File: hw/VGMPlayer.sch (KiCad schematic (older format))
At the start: 91 parts, among them J1 Micro_SD_Card, J2 EarPiece, P1 USB_C_Receptacle_16P, P2 SWD, P3 BATT, P4 UART, P5 ICSP, P6 CODEC, Q1 2N7002, Q2 AO3401A, Q3 2N7002, U1 RP2040, U2 W25QxxJVZP, U3 TPS79933DDCR, U4 WM8978, U5 TP4057, U6 PIC16F1503-IMG, U7 TPS79933DDCR, Y1 12MHz

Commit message: 2nd version, change KBC functions
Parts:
- removed P2: SWD, BZ_Connector:PINHDR-THT-50mil-01x05, symbol BZ_Connector:Conn_01x05
- removed P4: UART, BZ_Connector:PINHDR-THT-50mil-01x02, symbol BZ_Connector:Conn_01x02
- removed R20: 1K, BZ_Resistor:R_0402, symbol BZ_Passive:R
- removed U5: TP4057, BZ_Standard_IC:SOT-23-6, symbol BZ_PMIC:TP4057
- added M1: Mechanical-NC, BZ_Mechanical:Hole-Mech_0.5, symbol BZ_Misc:Mechanical-NC
- added P2: SWD, BZ_Connector:PINHDR-THT-50mil-02x05, symbol BZ_Connector:Conn_02x05
- added R25, R26: 1K, BZ_Resistor:R_0402, symbol BZ_Passive:R
- added S5: RESET, BZ_Switch:C&K_PTS525, symbol BZ_Switch:PB-SPST-NO_2P
- added U5: MCP73831-OT, BZ_Standard_IC:SOT-23-5, symbol BZ_Microchip:MCP73831-OT
- C24, C34: value 10n -> DNP
- C25: value 4.7u -> 10u; JLCPN C1705 -> (none); PN CL10A475KP8NNNC -> GRM188R61A106KE69D
- C3, C4: value 33p -> 22p
- C35: value 4.7u -> 10u; JLCPN C1705 -> (none); PN CL10A475KP8NNNC -> (none)
- R10, R9: value 2K -> 2K2
- R20: renamed from R21; value 2K -> 2K2
- TP1: footprint BZ_Misc:TE_RCT0805 -> BZ_Misc:TP_THT-Pad-0.8
- TP2: value BAT+ -> TP; footprint BZ_Misc:TE_RCT0805 -> BZ_Misc:TP_THT-Pad-0.8
- TP3: value BAT- -> TP; footprint BZ_Misc:TE_RCT0805 -> BZ_Misc:TP_THT-Pad-0.8
- U3, U7: value TPS79933DDCR -> LP5907MFX-3.3; symbol BZ_TI:TPS79933DDCR -> BZ_TI:LP5907MFX
- renumbered R22 to R21, R23 to R22, R24 to R23, R25 to R24
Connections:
- net labels removed: CHG_CHRG
- wire segments 367 -> 377
- no-connect marks 22 -> 23
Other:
- moved on the sheet: C1, R18, R19, R3, S4, TP1, U2

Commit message: Using Molex Picoblade 1.25 connector
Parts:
- removed P3: BATT, BZ_Connector:JST_SM02B-SRSS-TB, symbol BZ_Connector:Conn_01x02_MP
- added P3: BATT, BZ_Connector:MLX_PicoBlade-Horz-01x02-1.25P, symbol BZ_Connector:Conn_01x02
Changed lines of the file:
@@
 	2350 1050 2450 1050
-Wire Wire Line
-	3650 1600 3650 1950
 Wire Wire Line
 	2750 5900 2850 5900
@@
 	3550 1300 3550 1150
 Connection ~ 3550 1150
-Wire Wire Line
-	3550 1600 3550 2050
 $Comp
 L BZ_Passive:C C17
@@
 	1    0    0    -1
 $EndComp
-$Comp
-L BZ_Connector:Conn_01x02_MP P3
-U 1 1 60A279CB
-P 2650 1000
-F 0 "P3" H 2700 1000 40  0000 L CNN
-F 1 "BATT" H 2700 1050 40  0000 L CNN
-F 2 "BZ_Connector:JST_SM02B-SRSS-TB" H 2650 950 40  0001 C CNN
-F 3 "~" H 2650 950 40  0001 C CNN
-	1    2650 1000
-	1    0    0    1
-$EndComp
-$Comp
-L BZ_Power:GND #PWR0106
-U 1 1 60AACCCE
-P 2650 1200
-F 0 "#PWR0106" H 2650 1200 30  0001 C CNN
-F 1 "GND" H 2650 1130 30  0001 C CNN
-F 2 "" H 2650 1200 60  0001 C CNN
-F 3 "" H 2650 1200 60  0001 C CNN
-	1    2650 1200
-	1    0    0    -1
-$EndComp
 Connection ~ 2800 1700
 $Comp
@@
 Wire Wire Line
 	3950 1600 4000 1600
-Wire Wire Line
-	3550 2050 3450 2050
-Wire Wire Line
-	3450 1950 3650 1950
 Wire Wire Line
 	5450 6600 5900 6600
@@
 	1150 5400 1250 5400
 NoConn ~ 1250 5700
+Wire Wire Line
+	3550 1600 3550 1950
+$Comp
+L BZ_Connector:Conn_01x02 P3
+U 1 1 60C059FA
+P 2650 1000
+F 0 "P3" H 2700 950 40  0000 L CNN
+F 1 "BATT" H 2700 1050 40  0000 L CNN
+F 2 "BZ_Connector:MLX_PicoBlade-Horz-01x02-1.25P" H 2650 950 40  0001 C CNN
+F 3 "~" H 2650 950 40  0001 C CNN
+	1    2650 1000
+	1    0    0    -1
+$EndComp
+Wire Wire Line
+	3550 1950 3450 1950
+Wire Wire Line
+	3650 2050 3450 2050
+Wire Wire Line
+	3650 1600 3650 2050
 $EndSCHEMATC

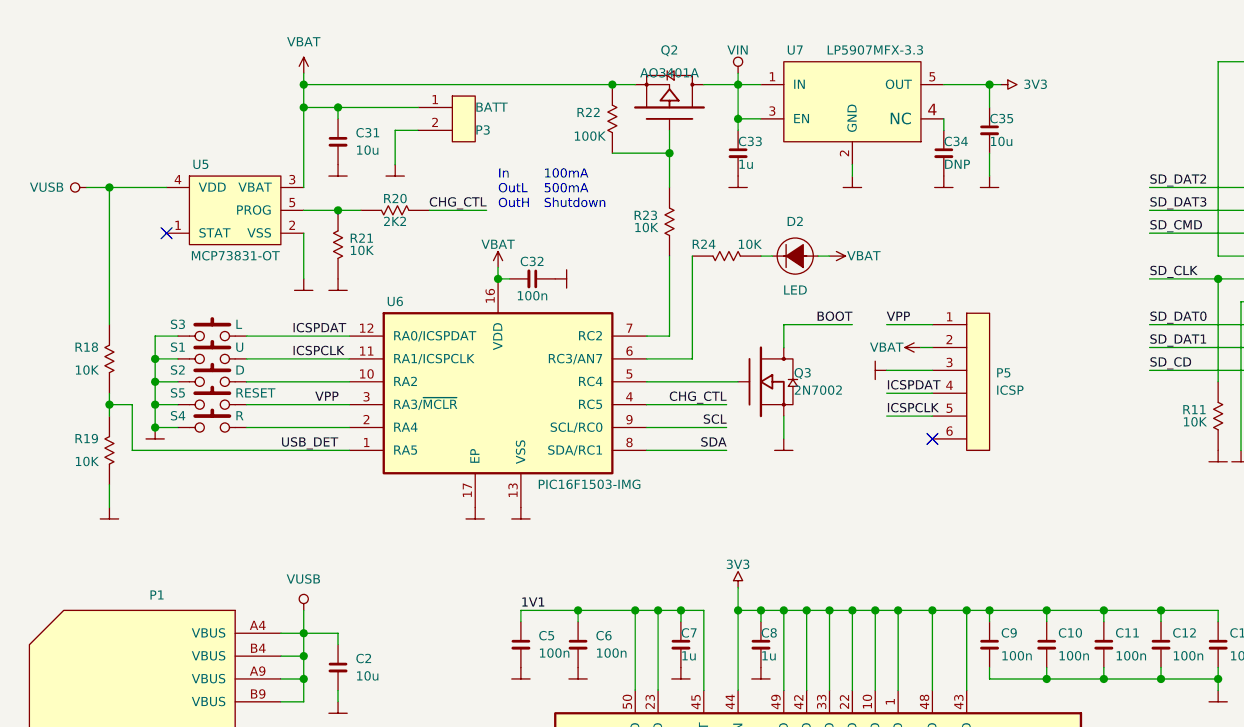
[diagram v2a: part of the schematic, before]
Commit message: USB/Batt power path
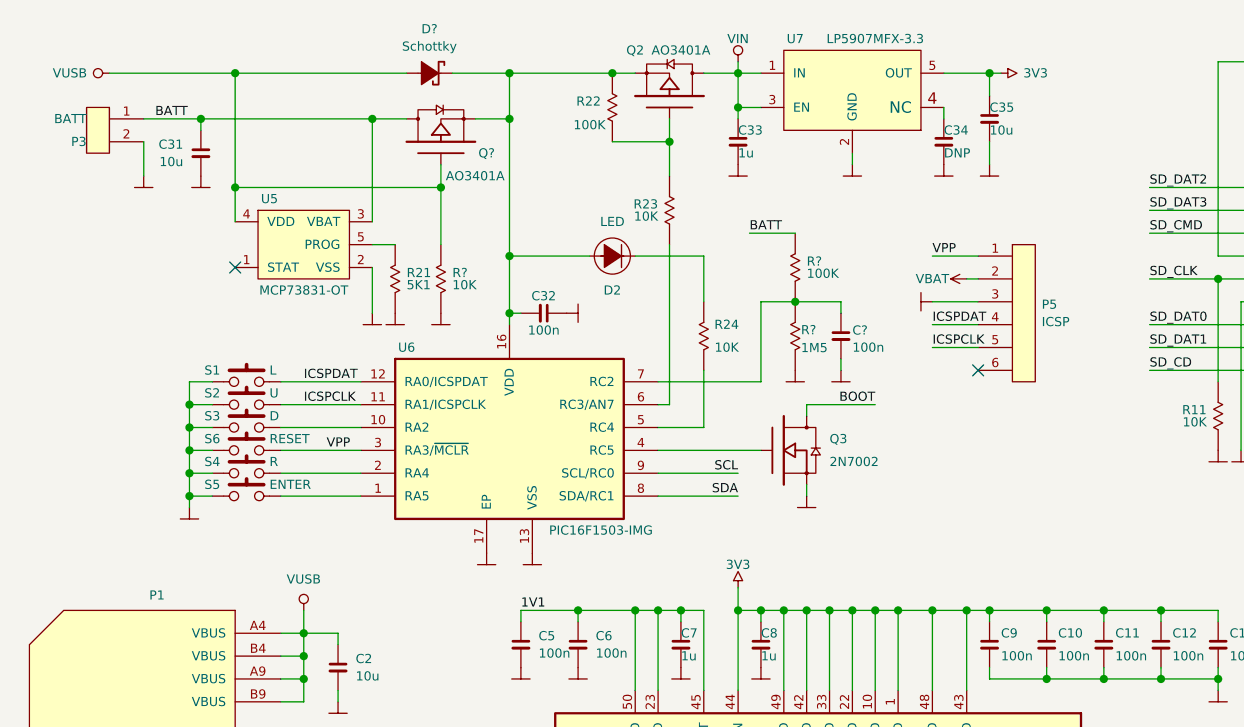
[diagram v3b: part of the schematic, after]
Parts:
- removed R18, R19: 10K, BZ_Resistor:R_0402, symbol BZ_Passive:R
- removed R20: 2K2, BZ_Resistor:R_0402, symbol BZ_Passive:R
- added C?: 100n, BZ_Capacitor:C_0402, symbol BZ_Passive:C
- added D?: Schottky, symbol BZ_Diode:Schottky
- added Q?: AO3401A, BZ_Standard_IC:SOT-23-3, symbol BZ_FET:MOS_P_GSD
- added R?: 10K, BZ_Resistor:R_0402, symbol BZ_Passive:R
- added R?: 100K, BZ_Resistor:R_0402, symbol BZ_Passive:R
- added R?: 1M5, BZ_Resistor:R_0402, symbol BZ_Passive:R
- added S5: ENTER, BZ_Switch:C&K_PTS525, symbol BZ_Switch:PB-SPST-NO_2P
- R21: value 10K -> 5K1
- renumbered S3 to S1, S1 to S2, S2 to S3, S5 to S6
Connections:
- net CHG_CTL is gone; now on an unnamed net: U6.4 (RC5)
- net GND: now also C?.2, R?.2, R?.2, S5.1
- net VBAT: no longer C31.1, C32.2, D2.A, P3.1 (Pin_1), Q2.2 (S), R22.1, U5.3 (VBAT), U6.16 (VDD)
- net VUSB: now also D?.A, Q?.1 (G), R?.1
- net at Q3.1 (G): no longer U6.5 (RC4)
- net at U6.6 (RC3/AN7): now also R23.2; no longer R24.2
- net at U6.7 (RC2): now also C?.1, R?.1, R?.2; no longer R23.2
- net at R24.1: now also U6.5 (RC4); no longer D2.K
- net USB_DET: no longer names the net of U6.1 (RA5)
- net USB_DET: now also S5.2
- new net: C32.2, D2.A, D?.K, Q2.2 (S), Q?.2 (S), R22.1, U6.16 (VDD)
- new net: D2.K, R24.2
- new net BATT: C31.1, P3.1 (Pin_1), Q?.3 (D), R?.1, U5.3 (VBAT)
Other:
- note removed: "100mA\n500mA\nShutdown"
- note removed: "In\nOutL\nOutH"
- moved on the sheet: C31, C32, C33, C34, C35, D2, P3, P5, Q2, Q3, R21, R22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

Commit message: Checkin before fab 20210610
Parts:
- D2: renamed from D?; value Schottky -> B0540WS; footprint (none) -> BZ_Diode:D_SOD-323
- S4: renamed from S5; value ENTER -> D
- S5: renamed from S3; value D -> ENTER
- S6: footprint BZ_Switch:C&K_PTS525 -> BZ_Switch:SW-PUSH_3x2x0.6H
- gave numbers to parts that had none: 5
- renumbered D2 to D3, Q1 to Q4, R21 to R18, R22 to R20, R23 to R21, R24 to R22, S4 to S2, S2 to S3
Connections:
- net BATT: now also TP2.1
- net GND: now also D3.K
- net VRAW: now reaches C32.2, D2.K, Q1.2 (S), Q2.2 (S), R20.1, U6.16 (VDD)
- net VRAW: now also P5.2 (Pin_2); no longer D3.A
- net at U6.6 (RC3/AN7): now also C36.1, R23.2, R24.1; no longer R21.2
- net at R22.2: now also D3.A; no longer D3.K
- removed net VBAT: P5.2 (Pin_2), TP2.1
- new net: R21.2, U6.7 (RC2)
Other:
- moved on the sheet: D3, Q3, R21, R22, TP2, TP3

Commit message: Sent for fab 20210610
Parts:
- R10, R9: value 2K2 -> 2.2K
- R18: value 5K1 -> 5.1K
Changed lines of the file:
@@
 	2250 1550 2350 1550
-$Comp
-L BZ_Passive:R R18
-U 1 1 6141459E
-P 2350 1700
-F 0 "R18" H 2400 1750 40  0000 L TNN
-F 1 "5K1" H 2400 1650 40  0000 L BNN
-F 2 "BZ_Resistor:R_0402" V 2280 1685 40  0001 C CNN
-F 3 "" H 2350 1685 40  0001 C CNN
-	1    2350 1700
-	1    0    0    -1
-$EndComp
 $Comp
 L BZ_Power:3V3 #PWR08
@@
 P 6050 5550
 F 0 "R9" H 6100 5600 40  0000 L TNN
-F 1 "2K2" H 6100 5500 40  0000 L BNN
+F 1 "2.2K" H 6100 5500 40  0000 L BNN
 F 2 "BZ_Resistor:R_0402" V 5980 5535 40  0001 C CNN
 F 3 "" H 6050 5535 40  0001 C CNN
@@
 P 6250 5550
 F 0 "R10" H 6300 5600 40  0000 L TNN
-F 1 "2K2" H 6300 5500 40  0000 L BNN
+F 1 "2.2K" H 6300 5500 40  0000 L BNN
 F 2 "BZ_Resistor:R_0402" V 6180 5535 40  0001 C CNN
 F 3 "" H 6250 5535 40  0001 C CNN
@@
 Wire Wire Line
 	4250 2350 4600 2350
+$Comp
+L BZ_Passive:R R18
+U 1 1 6141459E
+P 2350 1700
+F 0 "R18" H 2400 1750 40  0000 L TNN
+F 1 "5.1K" H 2400 1650 40  0000 L BNN
+F 2 "BZ_Resistor:R_0402" V 2280 1685 40  0001 C CNN
+F 3 "" H 2350 1685 40  0001 C CNN
+	1    2350 1700
+	1    0    0    -1
+$EndComp
 $EndSCHEMATC

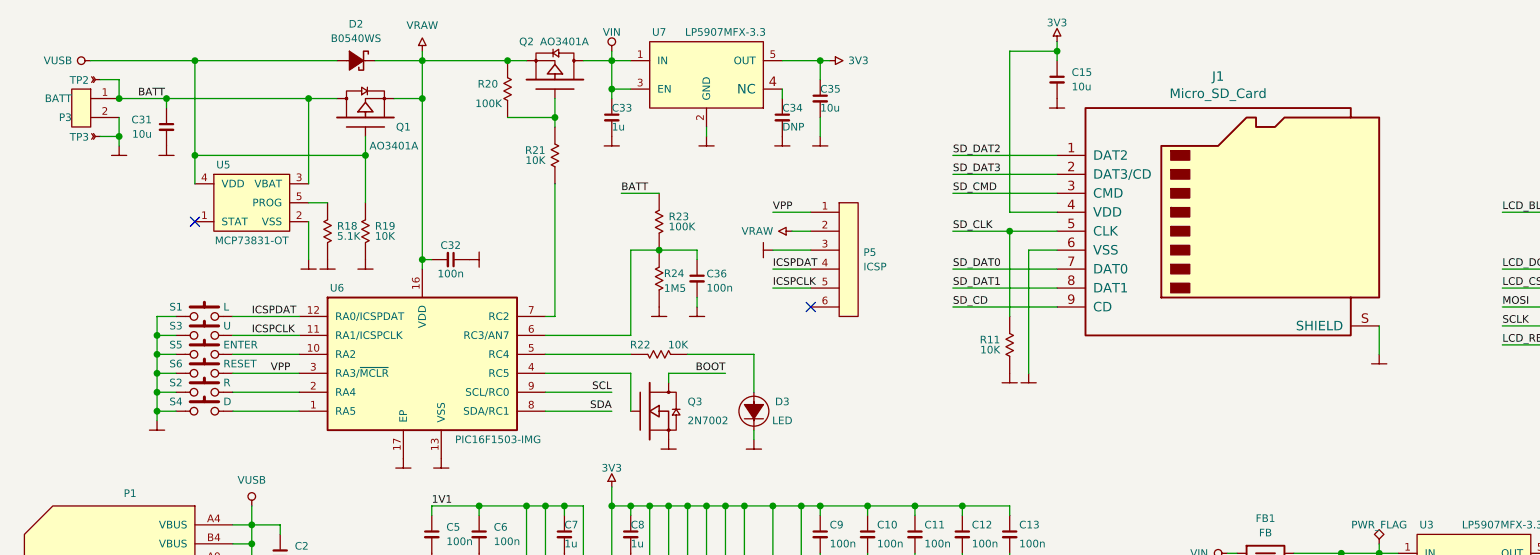
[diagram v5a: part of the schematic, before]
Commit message: Change to 4 buttons, layout adjust to casing design
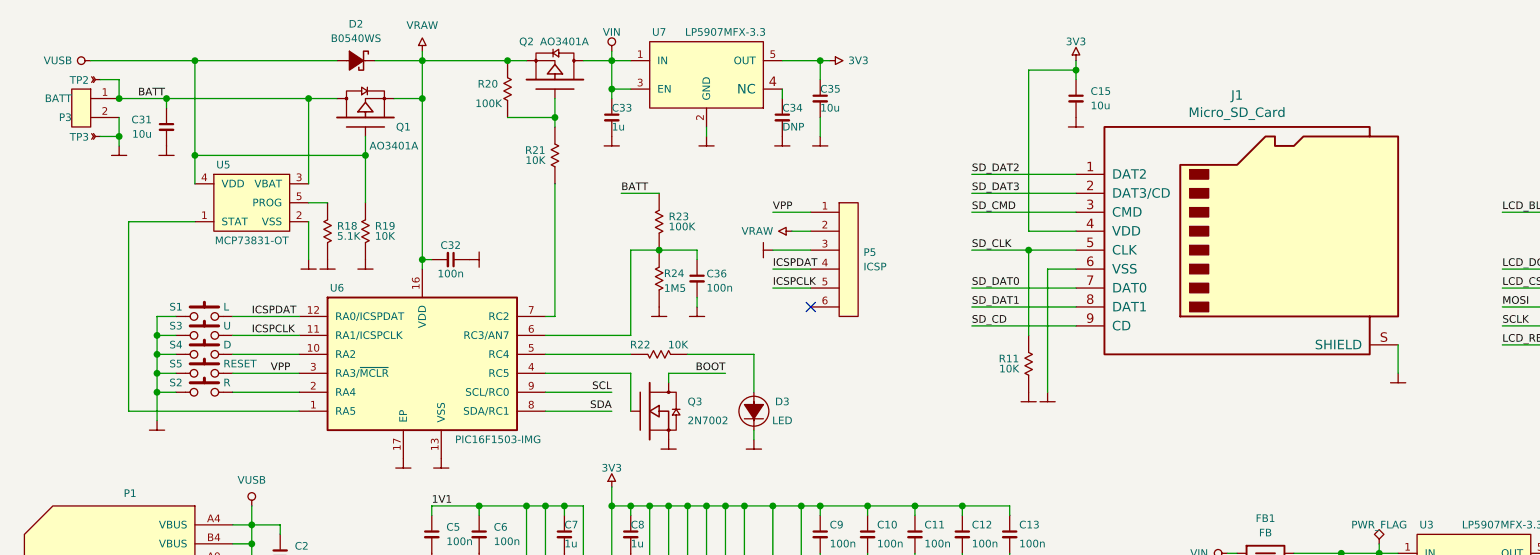
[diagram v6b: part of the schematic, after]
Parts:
- removed S5: ENTER, BZ_Switch:C&K_PTS525, symbol BZ_Switch:PB-SPST-NO_2P
- renumbered S6 to S5
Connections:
- net at U6.10 (RA2): now also S4.2
- net at U6.1 (RA5): now also U5.1 (STAT); no longer S4.2
- no-connect marks 23 -> 22
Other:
- moved on the sheet: C15, J1, R11, S4
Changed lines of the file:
@@
 	1    0    0    -1
 $EndComp
-Text Label 5650 2000 0    40   ~ 0
+Text Label 5750 2100 0    40   ~ 0
 SD_DAT1
 Wire Wire Line
-	5650 2000 6200 2000
-Text Label 5650 1300 0    40   ~ 0
+	5750 2100 6300 2100
+Text Label 5750 1400 0    40   ~ 0
 SD_DAT2
 Wire Wire Line
-	5650 1300 6200 1300
-Wire Wire Line
-	6200 800  6200 750
-Text Label 5650 1900 0    40   ~ 0
+	5750 1400 6300 1400
+Wire Wire Line
+	6300 900  6300 850
+Text Label 5750 2000 0    40   ~ 0
 SD_DAT0
-Text Label 5650 1700 0    40   ~ 0
+Text Label 5750 1800 0    40   ~ 0
 SD_CLK
-Text Label 5650 1500 0    40   ~ 0
+Text Label 5750 1600 0    40   ~ 0
 SD_CMD
-Text Label 5650 1400 0    40   ~ 0
+Text Label 5750 1500 0    40   ~ 0
 SD_DAT3
 $Comp
 L BZ_Power:GND #PWR020
 U 1 1 611C0CD1
-P 5950 2450
-F 0 "#PWR020" H 5950 2450 30  0001 C CNN
-F 1 "GND" H 5950 2380 30  0001 C CNN
-F 2 "" H 5950 2450 60  0001 C CNN
-F 3 "" H 5950 2450 60  0001 C CNN
-	1    5950 2450
+P 6050 2550
+F 0 "#PWR020" H 6050 2550 30  0001 C CNN
+F 1 "GND" H 6050 2480 30  0001 C CNN
+F 2 "" H 6050 2550 60  0001 C CNN
+F 3 "" H 6050 2550 60  0001 C CNN
+	1    6050 2550
 	1    0    0    -1
 $EndComp
@@
 L BZ_Passive:R R11
 U 1 1 611C0792
-P 5950 2300
-F 0 "R11" H 6000 2350 40  0000 L TNN
-F 1 "10K" H 6000 2250 40  0000 L BNN
-F 2 "BZ_Resistor:R_0402" V 5880 2285 40  0001 C CNN
-F 3 "" H 5950 2285 40  0001 C CNN
-	1    5950 2300
+P 6050 2400
+F 0 "R11" H 6100 2450 40  0000 L TNN
+F 1 "10K" H 6100 2350 40  0000 L BNN
+F 2 "BZ_Resistor:R_0402" V 5980 2385 40  0001 C CNN
+F 3 "" H 6050 2385 40  0001 C CNN
+	1    6050 2400
 	-1   0    0    -1
 $EndComp
 Wire Wire Line
-	5950 1700 5650 1700
-Wire Wire Line
-	5950 1700 5950 2150
-Wire Wire Line
-	6200 1900 5650 1900
-Wire Wire Line
-	6050 1800 6050 2450
+	6050 1800 5750 1800
+Wire Wire Line
+	6050 1800 6050 2250
+Wire Wire Line
+	6300 2000 5750 2000
+Wire Wire Line
+	6150 1900 6150 2550
 $Comp
 L BZ_Power:GND #PWR021
 U 1 1 61007FDC
-P 6050 2450
-F 0 "#PWR021" H 6050 2450 30  0001 C CNN
-F 1 "GND" H 6050 2380 30  0001 C CNN
-F 2 "" H 6050 2450 60  0001 C CNN
-F 3 "" H 6050 2450 60  0001 C CNN
-	1    6050 2450
-	1    0    0    -1
-$EndComp
-Wire Wire Line
-	6200 1800 6050 1800
-Wire Wire Line
-	6200 1700 5950 1700
-Wire Wire Line
-	6200 1500 5650 1500
-Wire Wire Line
-	6200 1400 5650 1400
-Connection ~ 6200 750
-Wire Wire Line
-	5950 1600 6200 1600
-Wire Wire Line
-	5950 750  5950 1600
-Wire Wire Line
-	6200 750  5950 750
-Wire Wire Line
-	6200 750  6200 700
+P 6150 2550
+F 0 "#PWR021" H 6150 2550 30  0001 C CNN
+F 1 "GND" H 6150 2480 30  0001 C CNN
+F 2 "" H 6150 2550 60  0001 C CNN
+F 3 "" H 6150 2550 60  0001 C CNN
+	1    6150 2550
+	1    0    0    -1
+$EndComp
+Wire Wire Line
+	6300 1900 6150 1900
+Wire Wire Line
+	6300 1800 6050 1800
+Wire Wire Line
+	6300 1600 5750 1600
+Wire Wire Line
+	6300 1500 5750 1500
+Connection ~ 6300 850
+Wire Wire Line
+	6050 1700 6300 1700
+Wire Wire Line
+	6050 850  6050 1700
+Wire Wire Line
+	6300 850  6050 850
+Wire Wire Line
+	6300 850  6300 800
 $Comp
 L BZ_Power:GND #PWR023
 U 1 1 60F50791
-P 6200 1000
-F 0 "#PWR023" H 6200 1000 30  0001 C CNN
-F 1 "GND" H 6200 930 30  0001 C CNN
-F 2 "" H 6200 1000 60  0001 C CNN
-F 3 "" H 6200 1000 60  0001 C CNN
-	1    6200 1000
+P 6300 1100
+F 0 "#PWR023" H 6300 1100 30  0001 C CNN
+F 1 "GND" H 6300 1030 30  0001 C CNN
+F 2 "" H 6300 1100 60  0001 C CNN
+F 3 "" H 6300 1100 60  0001 C CNN
+	1    6300 1100
 	1    0    0    -1
 $EndComp
@@
 L BZ_Passive:C C15
 U 1 1 60F244CE
-P 6200 900
-F 0 "C15" H 6277 938 40  0000 L CNN
-F 1 "10u" H 6277 862 40  0000 L CNN
-F 2 "BZ_Capacitor:C_0603" H 6200 900 40  0001 C CNN
-F 3 "" H 6200 900 40  0001 C CNN
-F 4 "GRM188R61A106KE69D " H 6200 900 50  0001 C CNN "PN"
-F 5 "C77044" H 6200 900 50  0001 C CNN "JLCPN"
-	1    6200 900
+P 6300 1000
+F 0 "C15" H 6377 1038 40  0000 L CNN
+F 1 "10u" H 6377 962 40  0000 L CNN
+F 2 "BZ_Capacitor:C_0603" H 6300 1000 40  0001 C CNN
+F 3 "" H 6300 1000 40  0001 C CNN
+F 4 "GRM188R61A106KE69D " H 6300 1000 50  0001 C CNN "PN"
+F 5 "C77044" H 6300 1000 50  0001 C CNN "JLCPN"
+	1    6300 1000
 	1    0    0    -1
 $EndComp
@@
 L BZ_Power:3V3 #PWR022
 U 1 1 60F23FFE
-P 6200 700
-F 0 "#PWR022" H 6200 660 40  0001 C CNN
-F 1 "3V3" H 6200 800 40  0000 C CNN
-F 2 "" H 6200 700 40  0001 C CNN
-F 3 "" H 6200 700 40  0001 C CNN
-	1    6200 700
-	1    0    0    -1
-$EndComp
-Wire Wire Line
-	7900 2350 7900 2200
+P 6300 800
+F 0 "#PWR022" H 6300 760 40  0001 C CNN
+F 1 "3V3" H 6300 900 40  0000 C CNN
+F 2 "" H 6300 800 40  0001 C CNN
+F 3 "" H 6300 800 40  0001 C CNN
+	1    6300 800
+	1    0    0    -1
+$EndComp
+Wire Wire Line
+	8000 2450 8000 2300
 $Comp
 L BZ_Power:GND #PWR024
 U 1 1 60EF7EE1
-P 7900 2350
-F 0 "#PWR024" H 7900 2350 30  0001 C CNN
-F 1 "GND" H 7900 2280 30  0001 C CNN
-F 2 "" H 7900 2350 60  0001 C CNN
-F 3 "" H 7900 2350 60  0001 C CNN
-	1    7900 2350
+P 8000 2450
+F 0 "#PWR024" H 8000 2450 30  0001 C CNN
+F 1 "GND" H 8000 2380 30  0001 C CNN
+F 2 "" H 8000 2450 60  0001 C CNN
+F 3 "" H 8000 2450 60  0001 C CNN
+	1    8000 2450
 	1    0    0    -1
 $EndComp
@@
 L BZ_Connector:Micro_SD_Card J1
 U 1 1 605B9496
-P 7100 1600
-F 0 "J1" H 7050 2317 50  0000 C CNN
-F 1 "Micro_SD_Card" H 7050 2226 50  0000 C CNN
-F 2 "BZ_Connector:XKB_XKTF-015-X" H 8250 1900 50  0001 C CNN
-F 3 "http://katalog.we-online.de/em/datasheet/693072010801.pdf" H 7100 1600 50  0001 C CNN
-	1    7100 1600
+P 7200 1700
+F 0 "J1" H 7150 2417 50  0000 C CNN
+F 1 "Micro_SD_Card" H 7150 2326 50  0000 C CNN
+F 2 "BZ_Connector:XKB_XKTF-015-X" H 8350 2000 50  0001 C CNN
+F 3 "http://katalog.we-online.de/em/datasheet/693072010801.pdf" H 7200 1700 50  0001 C CNN
+	1    7200 1700
 	1    0    0    -1
 $EndComp
@@
 F 3 "" H 1700 2150 40  0001 C CNN
 	1    1700 2150
-	1    0    0    -1
-$EndComp
-$Comp
-L BZ_Switch:PB-SPST-NO_2P S5
-U 1 1 606E4AE3
-P 1700 2350
-F 0 "S5" H 1550 2400 40  0000 C CNN
-F 1 "ENTER" H 1800 2400 40  0000 L CNN
-F 2 "BZ_Switch:C&K_PTS525" H 1700 2350 40  0001 C CNN
-F 3 "" H 1700 2350 40  0001 C CNN
-	1    1700 2350
 	1    0    0    -1
 $EndComp
@@
 	1450 2550 1550 2550
 Wire Wire Line
-	1550 2350 1450 2350
-Connection ~ 1450 2350
-Wire Wire Line
-	1450 2350 1450 2450
-Wire Wire Line
 	1550 2250 1450 2250
 Connection ~ 1450 2250
-Wire Wire Line
-	1450 2250 1450 2350
 Text Label 1950 2150 0    40   ~ 0
 ICSPDAT
 Text Label 1950 2250 0    40   ~ 0
 ICSPCLK
-Connection ~ 5950 1700
+Connection ~ 6050 1800
 Wire Wire Line
 	4950 1200 4950 1100
@@
 Wire Wire Line
 	1850 2250 2200 2250
-Wire Wire Line
-	1850 2350 2200 2350
 $Comp
 L BZ_Power:GND #PWR052
@@
 	9350 1500 9550 1500
 Wire Wire Line
-	6200 2100 5650 2100
+	6300 2200 5750 2200
 Wire Wire Line
 	5450 5100 5750 5100
-Text Label 5650 2100 0    40   ~ 0
+Text Label 5750 2200 0    40   ~ 0
 SD_CD
 Text Label 5750 5100 2    40   ~ 0
@@
 Wire Wire Line
 	1250 5250 1350 5250
-Wire Wire Line
-	1850 2650 2200 2650
 $Comp
 L BZ_Passive:C C4
@@
 Wire Wire Line
 	2600 5150 2950 5150
-NoConn ~ 1650 1650
 Wire Wire Line
 	2600 5550 2900 5550
@@
 	1850 2550 2200 2550
 $Comp
-L BZ_Switch:PB-SPST-NO_2P S6
+L BZ_Switch:PB-SPST-NO_2P S5
 U 1 1 613792FF
 P 1700 2450
-F 0 "S6" H 1550 2500 40  0000 C CNN
+F 0 "S5" H 1550 2500 40  0000 C CNN
 F 1 "RESET" H 1800 2500 40  0000 L CNN
 F 2 "BZ_Switch:SW-PUSH_3x2x0.6H" H 1700 2450 40  0001 C CNN
@@
 L BZ_Switch:PB-SPST-NO_2P S4
 U 1 1 61B88515
-P 1700 2650
-F 0 "S4" H 1550 2700 40  0000 C CNN
-F 1 "D" H 1800 2700 40  0000 L CNN
-F 2 "BZ_Switch:C&K_PTS525" H 1700 2650 40  0001 C CNN
-F 3 "" H 1700 2650 40  0001 C CNN
-	1    1700 2650
+P 1700 2350
+F 0 "S4" H 1550 2400 40  0000 C CNN
+F 1 "D" H 1800 2400 40  0000 L CNN
+F 2 "BZ_Switch:C&K_PTS525" H 1700 2350 40  0001 C CNN
+F 3 "" H 1700 2350 40  0001 C CNN
+	1    1700 2350
 	1    0    0    -1
 $EndComp
@@
 	1    0    0    -1
 $EndComp
-Wire Wire Line
-	1550 2650 1450 2650
-Wire Wire Line
-	1450 2650 1450 2700
-Wire Wire Line
-	1450 2550 1450 2650
 Connection ~ 1450 2550
-Connection ~ 1450 2650
 $Comp
 L BZ_Passive:C C36
@@
 	1    0    0    -1
 $EndComp
+Wire Wire Line
+	1450 2250 1450 2350
+Wire Wire Line
+	1300 1650 1650 1650
+Wire Wire Line
+	1850 2350 2200 2350
+Wire Wire Line
+	1550 2350 1450 2350
+Connection ~ 1450 2350
+Wire Wire Line
+	1450 2350 1450 2450
+Wire Wire Line
+	1450 2550 1450 2700
+Wire Wire Line
+	1300 2650 2200 2650
+Wire Wire Line
+	1300 1650 1300 2650
 $EndSCHEMATC
